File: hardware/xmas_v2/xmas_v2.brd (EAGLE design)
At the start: 160 x 100 mm, 0 parts

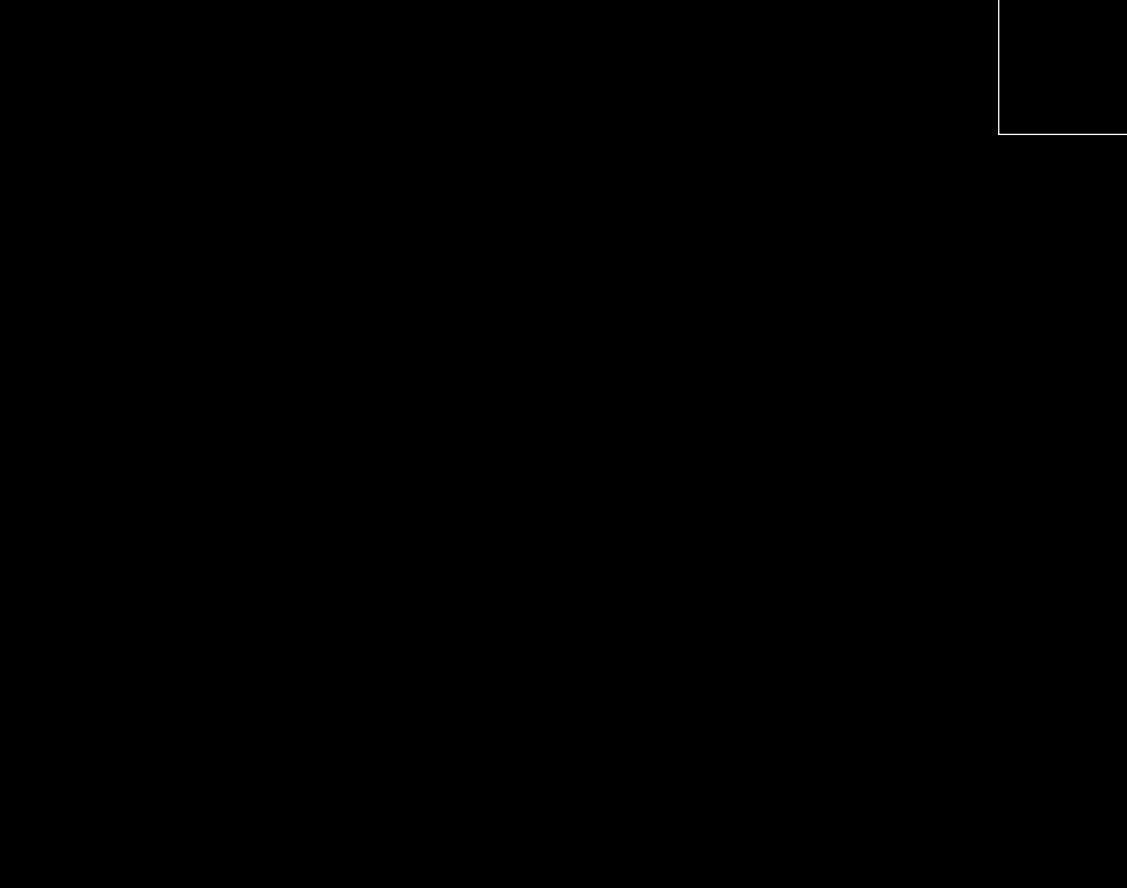
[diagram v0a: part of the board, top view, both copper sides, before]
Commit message: Added all parts
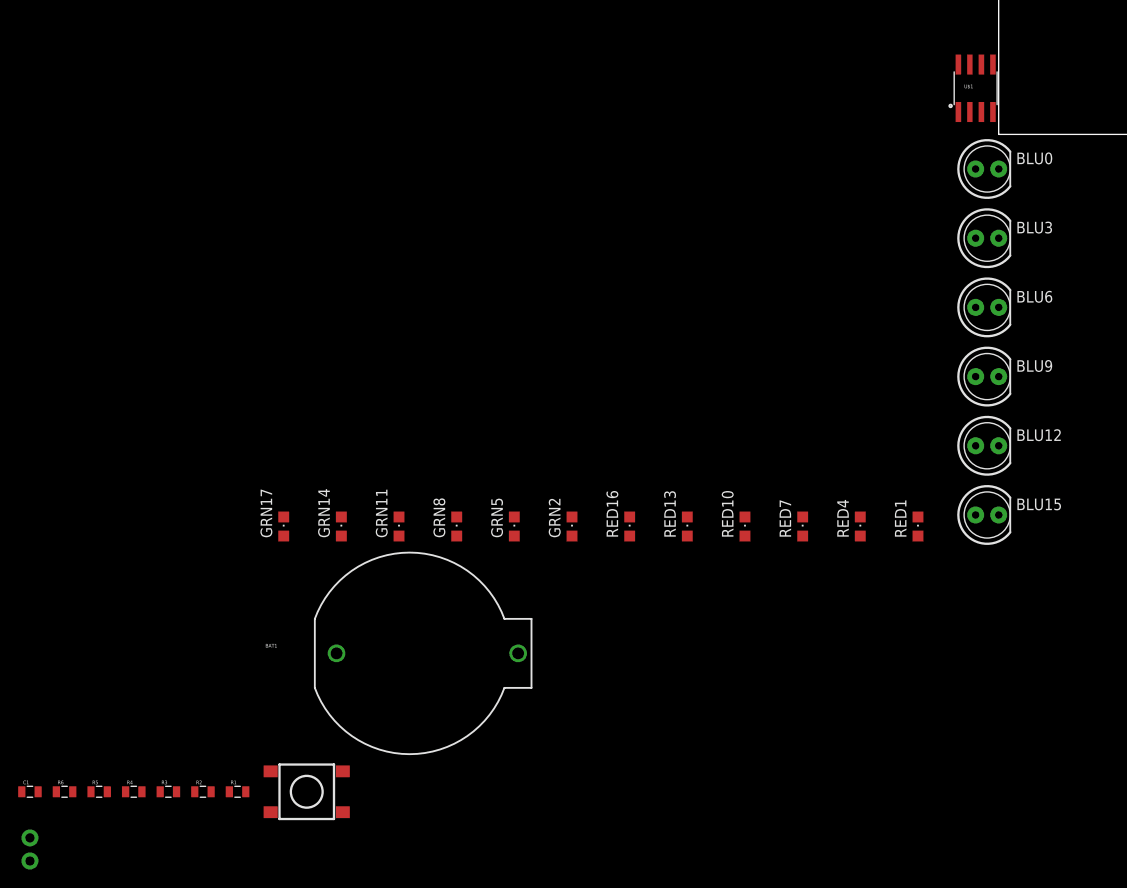
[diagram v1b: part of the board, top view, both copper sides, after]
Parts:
- added BAT1: 3V, SparkFun-Electromechanical:BATTCOM_20MM_PTH
- added BLU0, BLU12, BLU15, BLU3, BLU6, BLU9: (no value), SparkFun-LED:LED5MM-KIT
- added C1: .1uf, SparkFun-Capacitors:0805
- added GRN11, GRN14, GRN17, GRN2, GRN5, GRN8, RED1, RED10, RED13, RED16, RED4, RED7: (no value), adafruit:CHIPLED_0805
- added JP1, JP2: (no value), SparkFun-Connectors:1X01NS-KIT
- added R1, R2, R3, R4, R5: 100, SparkFun-Passives:0805
- added R6: 10K, SparkFun-Passives:0805
- added S1: SWITCH-MOMENTARY-2SMD-4, SparkFun-Electromechanical:TACTILE_SWITCH_TALL
- added U$1: ATTINY13SOIC, SparkFun-DigitalIC:SO08
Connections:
- new net +: BAT1.1
- new net -: BAT1.2
- new net PB0: BLU9.A, GRN11.A, GRN8.A, RED10.A
- new net PB1: BLU12.A, BLU15.A, GRN14.A, RED13.A
- new net PB2: GRN17.A, RED16.A
- new net PB3: BLU0.A, BLU3.A, GRN2.A, RED1.A
- new net PB4: BLU6.A, GRN5.A, RED4.A, RED7.A

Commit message: Added charlieplex schem
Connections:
- new net N$1: BLU0.A, BLU3.A, GRN2.A, R1.2, RED1.A
- new net N$2: BLU6.A, GRN5.A, R2.2, RED4.A, RED7.A
- new net N$3: BLU9.A, GRN11.A, GRN8.A, R3.2, RED10.A
- new net N$4: BLU12.A, BLU15.A, GRN14.A, R4.2, RED13.A
- new net N$5: GRN17.A, R5.2, RED16.A
- net PB0: now also GRN14.C, GRN5.C, R3.1, RED1.C; no longer BLU9.A, GRN11.A, GRN8.A, RED10.A
- net PB1: now also BLU6.K, GRN2.C, R4.1, RED10.C; no longer BLU12.A, BLU15.A, GRN14.A, RED13.A
- net PB2: now also BLU15.K, BLU3.K, GRN11.C, R5.1, RED7.C; no longer GRN17.A, RED16.A
- net PB3: now also BLU12.K, GRN8.C, R1.1, RED16.C, RED4.C; no longer BLU0.A, BLU3.A, GRN2.A, RED1.A
- net PB4: now also BLU0.K, BLU9.K, GRN17.C, R2.1, RED13.C; no longer BLU6.A, GRN5.A, RED4.A, RED7.A
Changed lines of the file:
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@@
 <contactref element="BAT1" pad="1"/>
 </signal>
-<signal name="PB3">
+<signal name="N$1">
 <contactref element="BLU3" pad="A"/>
 <contactref element="BLU0" pad="A"/>
 <contactref element="RED1" pad="A"/>
 <contactref element="GRN2" pad="A"/>
+<contactref element="R1" pad="2"/>
+<wire x1="-46.99" y1="-44.23" x2="-82.92" y2="-72.39" width="0" layer="19" extent="1-1"/>
 <wire x1="-8.89" y1="-44.23" x2="-46.99" y2="-44.23" width="0" layer="19" extent="1-1"/>
 <wire x1="-2.54" y1="-11.43" x2="-8.89" y2="-44.23" width="0" layer="19" extent="1-1"/>
 <wire x1="-2.54" y1="-3.81" x2="-2.54" y2="-11.43" width="0" layer="19" extent="1-1"/>
 </signal>
-<signal name="PB4">
+<signal name="N$2">
 <contactref element="RED7" pad="A"/>
 <contactref element="RED4" pad="A"/>
 <contactref element="GRN5" pad="A"/>
 <contactref element="BLU6" pad="A"/>
+<contactref element="R2" pad="2"/>
+<wire x1="-53.34" y1="-44.23" x2="-86.73" y2="-72.39" width="0" layer="19" extent="1-1"/>
 <wire x1="-21.59" y1="-44.23" x2="-53.34" y2="-44.23" width="0" layer="19" extent="1-1"/>
 <wire x1="-15.24" y1="-44.23" x2="-21.59" y2="-44.23" width="0" layer="19" extent="1-1"/>
 <wire x1="-2.54" y1="-19.05" x2="-15.24" y2="-44.23" width="0" layer="19" extent="1-1"/>
 </signal>
-<signal name="PB0">
+<signal name="N$3">
 <contactref element="GRN11" pad="A"/>
 <contactref element="GRN8" pad="A"/>
 <contactref element="BLU9" pad="A"/>
 <contactref element="RED10" pad="A"/>
+<contactref element="R3" pad="2"/>
+<wire x1="-66.04" y1="-44.23" x2="-90.54" y2="-72.39" width="0" layer="19" extent="1-1"/>
 <wire x1="-59.69" y1="-44.23" x2="-66.04" y2="-44.23" width="0" layer="19" extent="1-1"/>
 <wire x1="-27.94" y1="-44.23" x2="-59.69" y2="-44.23" width="0" layer="19" extent="1-1"/>
 <wire x1="-2.54" y1="-26.67" x2="-27.94" y2="-44.23" width="0" layer="19" extent="1-1"/>
 </signal>
-<signal name="PB1">
+<signal name="N$4">
 <contactref element="BLU15" pad="A"/>
 <contactref element="BLU12" pad="A"/>
 <contactref element="RED13" pad="A"/>
 <contactref element="GRN14" pad="A"/>
+<contactref element="R4" pad="2"/>
+<wire x1="-72.39" y1="-44.23" x2="-94.35" y2="-72.39" width="0" layer="19" extent="1-1"/>
 <wire x1="-34.29" y1="-44.23" x2="-72.39" y2="-44.23" width="0" layer="19" extent="1-1"/>
 <wire x1="-2.54" y1="-41.91" x2="-34.29" y2="-44.23" width="0" layer="19" extent="1-1"/>
 <wire x1="-2.54" y1="-34.29" x2="-2.54" y2="-41.91" width="0" layer="19" extent="1-1"/>
 </signal>
-<signal name="PB2">
+<signal name="N$5">
 <contactref element="GRN17" pad="A"/>
 <contactref element="RED16" pad="A"/>
+<contactref element="R5" pad="2"/>
+<wire x1="-78.74" y1="-44.23" x2="-98.16" y2="-72.39" width="0" layer="19" extent="1-1"/>
 <wire x1="-40.64" y1="-44.23" x2="-78.74" y2="-44.23" width="0" layer="19" extent="1-1"/>
 </signal>
+<signal name="PB0">
+<contactref element="RED1" pad="C"/>
+<contactref element="GRN5" pad="C"/>
+<contactref element="R3" pad="1"/>
+<contactref element="GRN14" pad="C"/>
+<wire x1="-72.39" y1="-42.13" x2="-92.34" y2="-72.39" width="0" layer="19" extent="1-1"/>
+<wire x1="-53.34" y1="-42.13" x2="-72.39" y2="-42.13" width="0" layer="19" extent="1-1"/>
+<wire x1="-8.89" y1="-42.13" x2="-53.34" y2="-42.13" width="0" layer="19" extent="1-1"/>
+</signal>
+<signal name="PB1">
+<contactref element="GRN2" pad="C"/>
+<contactref element="BLU6" pad="K"/>
+<contactref element="RED10" pad="C"/>
+<contactref element="R4" pad="1"/>
+<wire x1="-46.99" y1="-42.13" x2="-96.15" y2="-72.39" width="0" layer="19" extent="1-1"/>
+<wire x1="-27.94" y1="-42.13" x2="-46.99" y2="-42.13" width="0" layer="19" extent="1-1"/>
+<wire x1="0" y1="-19.05" x2="-27.94" y2="-42.13" width="0" layer="19" extent="1-1"/>
+</signal>
+<signal name="PB2">
+<contactref element="BLU3" pad="K"/>
+<contactref element="RED7" pad="C"/>
+<contactref element="GRN11" pad="C"/>
+<contactref element="BLU15" pad="K"/>
+<contactref element="R5" pad="1"/>
+<wire x1="-66.04" y1="-42.13" x2="-99.96" y2="-72.39" width="0" layer="19" extent="1-1"/>
+<wire x1="-21.59" y1="-42.13" x2="-66.04" y2="-42.13" width="0" layer="19" extent="1-1"/>
+<wire x1="0" y1="-41.91" x2="-21.59" y2="-42.13" width="0" layer="19" extent="1-1"/>
+<wire x1="0" y1="-11.43" x2="0" y2="-41.91" width="0" layer="19" extent="1-1"/>
+</signal>
+<signal name="PB4">
+<contactref element="BLU0" pad="K"/>
+<contactref element="R2" pad="1"/>
+<contactref element="BLU9" pad="K"/>
+<contactref element="RED13" pad="C"/>
+<contactref element="GRN17" pad="C"/>
+<wire x1="-78.74" y1="-42.13" x2="-88.53" y2="-72.39" width="0" layer="19" extent="1-1"/>
+<wire x1="-34.29" y1="-42.13" x2="-78.74" y2="-42.13" width="0" layer="19" extent="1-1"/>
+<wire x1="0" y1="-26.67" x2="-34.29" y2="-42.13" width="0" layer="19" extent="1-1"/>
+<wire x1="0" y1="-3.81" x2="0" y2="-26.67" width="0" layer="19" extent="1-1"/>
+</signal>
+<signal name="PB3">
+<contactref element="R1" pad="1"/>
+<contactref element="RED4" pad="C"/>
+<contactref element="GRN8" pad="C"/>
+<contactref element="BLU12" pad="K"/>
+<contactref element="RED16" pad="C"/>
+<wire x1="-59.69" y1="-42.13" x2="-84.72" y2="-72.39" width="0" layer="19" extent="1-1"/>
+<wire x1="-40.64" y1="-42.13" x2="-59.69" y2="-42.13" width="0" layer="19" extent="1-1"/>
+<wire x1="-15.24" y1="-42.13" x2="-40.64" y2="-42.13" width="0" layer="19" extent="1-1"/>
+<wire x1="0" y1="-34.29" x2="-15.24" y2="-42.13" width="0" layer="19" extent="1-1"/>
+</signal>
 </signals>

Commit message: Schematic is done
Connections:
- removed net +: BAT1.1
- removed net -: BAT1.2
- new net GND: BAT1.2, C1.2, JP1.1, JP2.1, R6.1, U$1.4
- new net N$10: R6.2, S1.A2, U$1.1
- new net VCC: BAT1.1, C1.1, S1.B2, U$1.8
- net PB0: now also U$1.5
- net PB1: now also U$1.6
- net PB2: now also U$1.7
- net PB3: now also U$1.2
- net PB4: now also U$1.3
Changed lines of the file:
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@@
 </elements>
 <signals>
-<signal name="-">
-<contactref element="BAT1" pad="2"/>
-</signal>
-<signal name="+">
-<contactref element="BAT1" pad="1"/>
-</signal>
 <signal name="N$1">
 <contactref element="BLU3" pad="A"/>
@@
 <contactref element="R3" pad="1"/>
 <contactref element="GRN14" pad="C"/>
+<contactref element="U$1" pad="5"/>
 <wire x1="-72.39" y1="-42.13" x2="-92.34" y2="-72.39" width="0" layer="19" extent="1-1"/>
 <wire x1="-53.34" y1="-42.13" x2="-72.39" y2="-42.13" width="0" layer="19" extent="1-1"/>
 <wire x1="-8.89" y1="-42.13" x2="-53.34" y2="-42.13" width="0" layer="19" extent="1-1"/>
+<wire x1="-0.635" y1="7.6962" x2="-8.89" y2="-42.13" width="0" layer="19" extent="1-1"/>
 </signal>
 <signal name="PB1">
@@
 <contactref element="RED10" pad="C"/>
 <contactref element="R4" pad="1"/>
+<contactref element="U$1" pad="6"/>
 <wire x1="-46.99" y1="-42.13" x2="-96.15" y2="-72.39" width="0" layer="19" extent="1-1"/>
 <wire x1="-27.94" y1="-42.13" x2="-46.99" y2="-42.13" width="0" layer="19" extent="1-1"/>
 <wire x1="0" y1="-19.05" x2="-27.94" y2="-42.13" width="0" layer="19" extent="1-1"/>
+<wire x1="-1.905" y1="7.6962" x2="0" y2="-19.05" width="0" layer="19" extent="1-1"/>
 </signal>
 <signal name="PB2">
@@
 <contactref element="BLU15" pad="K"/>
 <contactref element="R5" pad="1"/>
+<contactref element="U$1" pad="7"/>
 <wire x1="-66.04" y1="-42.13" x2="-99.96" y2="-72.39" width="0" layer="19" extent="1-1"/>
 <wire x1="-21.59" y1="-42.13" x2="-66.04" y2="-42.13" width="0" layer="19" extent="1-1"/>
 <wire x1="0" y1="-41.91" x2="-21.59" y2="-42.13" width="0" layer="19" extent="1-1"/>
 <wire x1="0" y1="-11.43" x2="0" y2="-41.91" width="0" layer="19" extent="1-1"/>
+<wire x1="-3.175" y1="7.6962" x2="0" y2="-11.43" width="0" layer="19" extent="1-1"/>
 </signal>
 <signal name="PB4">
@@
 <contactref element="RED13" pad="C"/>
 <contactref element="GRN17" pad="C"/>
+<contactref element="U$1" pad="3"/>
 <wire x1="-78.74" y1="-42.13" x2="-88.53" y2="-72.39" width="0" layer="19" extent="1-1"/>
 <wire x1="-34.29" y1="-42.13" x2="-78.74" y2="-42.13" width="0" layer="19" extent="1-1"/>
 <wire x1="0" y1="-26.67" x2="-34.29" y2="-42.13" width="0" layer="19" extent="1-1"/>
 <wire x1="0" y1="-3.81" x2="0" y2="-26.67" width="0" layer="19" extent="1-1"/>
+<wire x1="-1.905" y1="2.4638" x2="0" y2="-3.81" width="0" layer="19" extent="1-1"/>
 </signal>
 <signal name="PB3">
@@
 <contactref element="BLU12" pad="K"/>
 <contactref element="RED16" pad="C"/>
+<contactref element="U$1" pad="2"/>
 <wire x1="-59.69" y1="-42.13" x2="-84.72" y2="-72.39" width="0" layer="19" extent="1-1"/>
 <wire x1="-40.64" y1="-42.13" x2="-59.69" y2="-42.13" width="0" layer="19" extent="1-1"/>
 <wire x1="-15.24" y1="-42.13" x2="-40.64" y2="-42.13" width="0" layer="19" extent="1-1"/>
 <wire x1="0" y1="-34.29" x2="-15.24" y2="-42.13" width="0" layer="19" extent="1-1"/>
+<wire x1="-3.175" y1="2.4638" x2="0" y2="-34.29" width="0" layer="19" extent="1-1"/>
+</signal>
+<signal name="VCC">
+<contactref element="U$1" pad="8"/>
+<contactref element="BAT1" pad="1"/>
+<contactref element="C1" pad="1"/>
+<contactref element="S1" pad="B2"/>
+<wire x1="-72.225" y1="-70.14" x2="-107.58" y2="-72.39" width="0" layer="19" extent="1-1"/>
+<wire x1="-52.92" y1="-57.15" x2="-72.225" y2="-70.14" width="0" layer="19" extent="1-1"/>
+<wire x1="-4.445" y1="7.6962" x2="-52.92" y2="-57.15" width="0" layer="19" extent="1-1"/>
+</signal>
+<signal name="GND">
+<contactref element="U$1" pad="4"/>
+<contactref element="C1" pad="2"/>
+<contactref element="BAT1" pad="2"/>
+<contactref element="JP2" pad="1"/>
+<contactref element="JP1" pad="1"/>
+<contactref element="R6" pad="1"/>
+<wire x1="-106.68" y1="-77.47" x2="-106.68" y2="-80.01" width="0" layer="19" extent="1-1"/>
+<wire x1="-105.78" y1="-72.39" x2="-106.68" y2="-77.47" width="0" layer="19" extent="1-1"/>
+<wire x1="-103.77" y1="-72.39" x2="-105.78" y2="-72.39" width="0" layer="19" extent="1-1"/>
+<wire x1="-72.92" y1="-57.15" x2="-103.77" y2="-72.39" width="0" layer="19" extent="1-1"/>
+<wire x1="-0.635" y1="2.4638" x2="-72.92" y2="-57.15" width="0" layer="19" extent="1-1"/>
+</signal>
+<signal name="N$10">
+<contactref element="R6" pad="2"/>
+<contactref element="U$1" pad="1"/>
+<contactref element="S1" pad="A2"/>
+<wire x1="-72.225" y1="-74.64" x2="-101.97" y2="-72.39" width="0" layer="19" extent="1-1"/>
+<wire x1="-4.445" y1="2.4638" x2="-72.225" y2="-74.64" width="0" layer="19" extent="1-1"/>
 </signal>
 </signals>

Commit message: Added PCB outline
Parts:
- moved BAT1 108.3 mm to (-20.8, 41.9)
- moved C1 102.4 mm to (-46.7, 10.6)
- moved JP1 102.4 mm to (-46.7, 5.53)
- moved JP2 102.4 mm to (-46.7, 2.99)
- moved R1 102.4 mm to (-23.8, 10.6)
- moved R2 102.4 mm to (-27.6, 10.6)
- moved R3 102.4 mm to (-31.4, 10.6)
- moved R4 102.4 mm to (-35.2, 10.6)
- moved R5 102.4 mm to (-39.1, 10.6)
- moved R6 102.4 mm to (-42.9, 10.6)
- moved S1 102.4 mm to (-16.2, 10.6)
- moved BLU15 79.9 mm to (-48.9, 22.3), turned to 270 degrees
- moved BLU12 69.3 mm to (-41.3, 22.3), turned to 270 degrees
- moved BLU9 58.7 mm to (-33.7, 22.3), turned to 270 degrees
- moved U$1 56.6 mm to (-44.5, 43.1)
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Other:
- board size 160 x 100 mm -> 50 x 50 mm

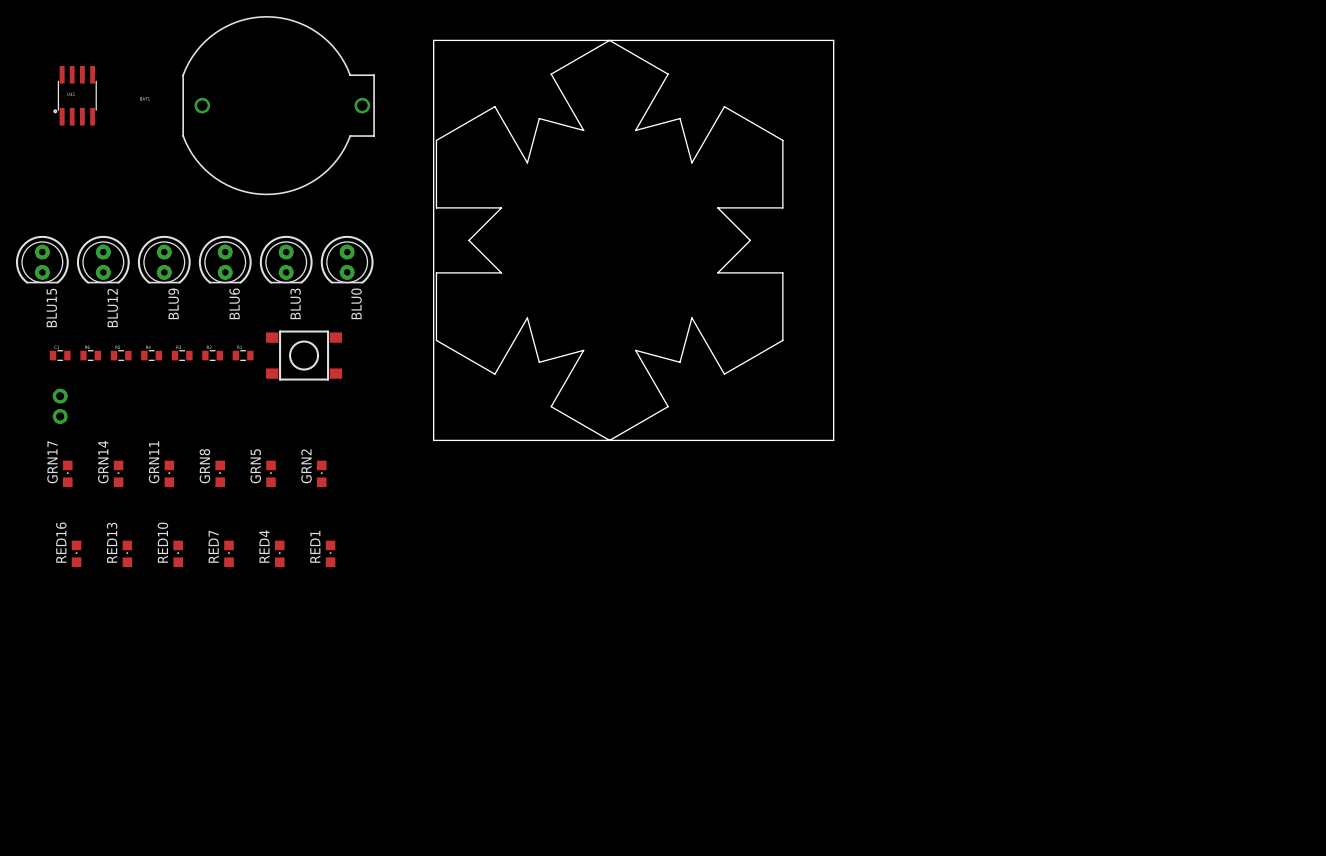
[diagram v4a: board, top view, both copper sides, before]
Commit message: All LEDs and most parts have been aligned
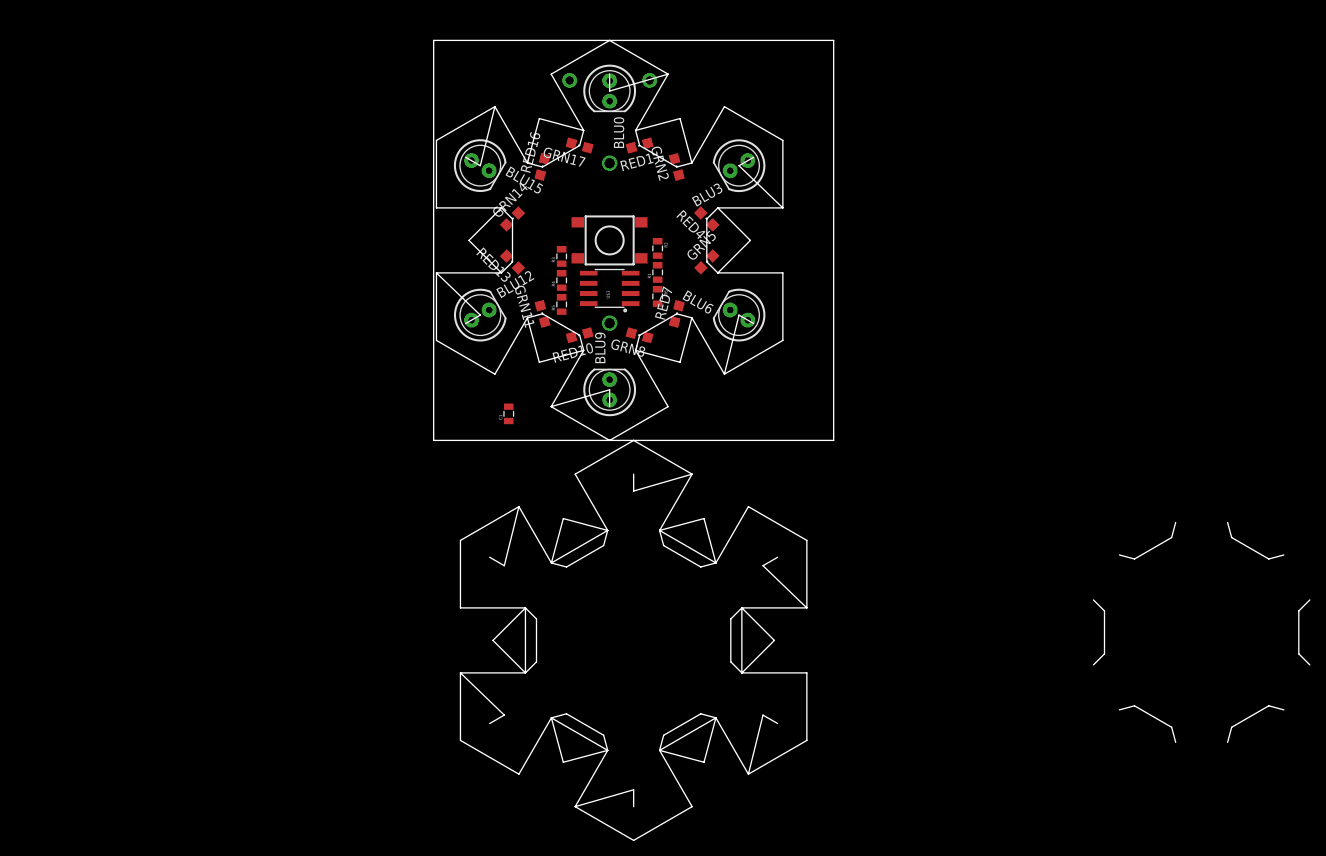
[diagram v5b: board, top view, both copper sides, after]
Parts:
- moved JP1 83.6 mm to (27.0, 45.0)
- moved JP2 76.3 mm to (17.0, 45.0)
- moved GRN17 76.0 mm to (18.2, 36.9), turned to 75 degrees
- moved RED16 75.7 mm to (13.6, 34.2), turned to 345 degrees
- moved R6 71.3 mm to (28.0, 18.0), turned to 270 degrees
- moved U$1 70.8 mm to (22.0, 19.0), turned to 90 degrees
- moved RED4 67.8 mm to (34.1, 27.7), turned to 45 degrees
- moved BLU6 64.6 mm to (38.2, 15.7), turned to 150 degrees
- moved RED1 64.0 mm to (25.8, 36.9), turned to 105 degrees
- moved RED7 63.5 mm to (30.4, 15.8), turned to 345 degrees
- moved GRN5 60.6 mm to (34.1, 22.3), turned to 315 degrees
- moved RED13 60.4 mm to (9.86, 22.3), turned to 45 degrees
- moved GRN2 58.7 mm to (30.4, 34.2), turned to 15 degrees
- moved GRN14 58.7 mm to (9.86, 27.7), turned to 315 degrees
- moved BLU9 57.9 mm to (22.0, 6.33), turned to 90 degrees
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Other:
- board size 50 x 50 mm -> 109.5 x 100 mm
